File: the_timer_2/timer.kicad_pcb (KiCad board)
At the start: 4 copper layers, 24 x 75 mm, 117 parts, among them J1 Screw_Terminal_01x06, J3 BMI-S-209-F, J4 Screw_Terminal_01x06, J5 R41-B583A, J6 BMI-S-209-F, J7 Screw_Terminal_01x02, Q1 AS2312, Q2 AS2312, Q3 AS2312, Q4 AS2312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

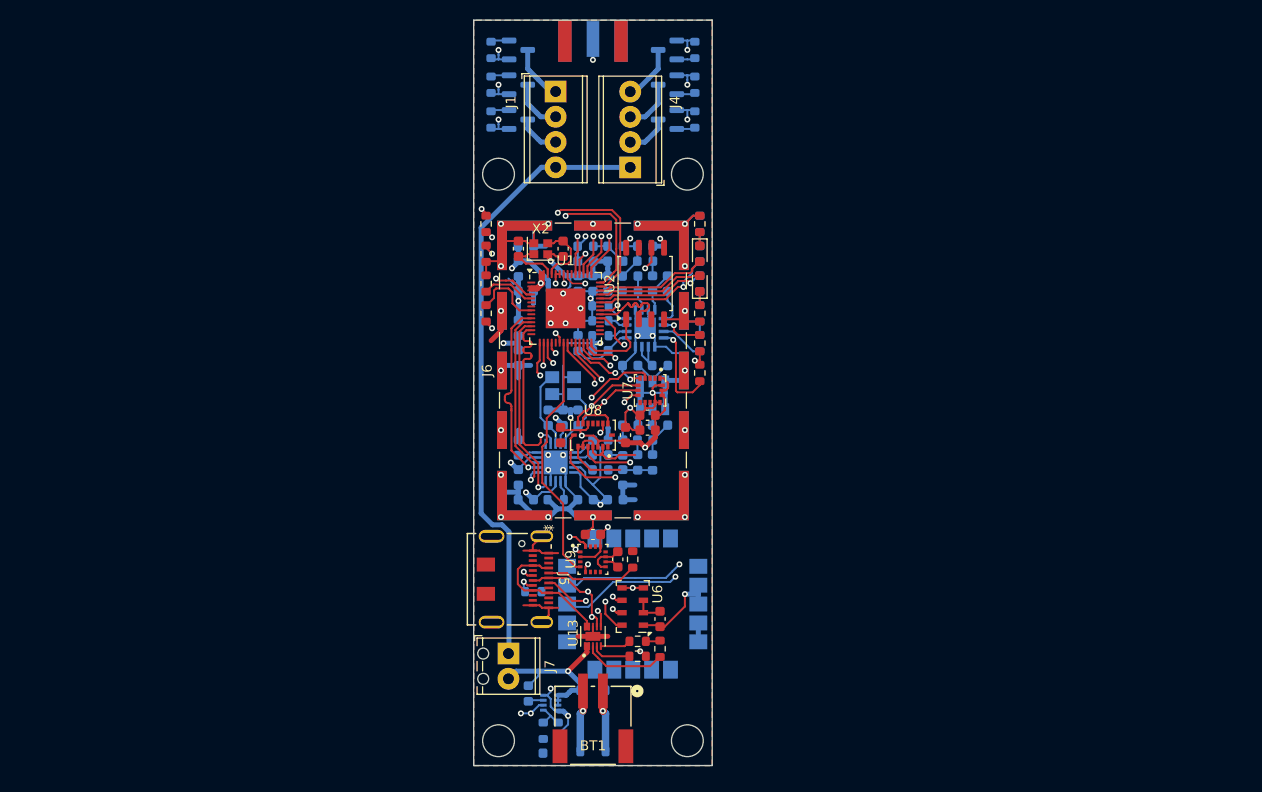
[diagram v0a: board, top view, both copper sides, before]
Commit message: Mostly de-exploded the schematic
Also like sorta fixed the PCB design but not really but sorta
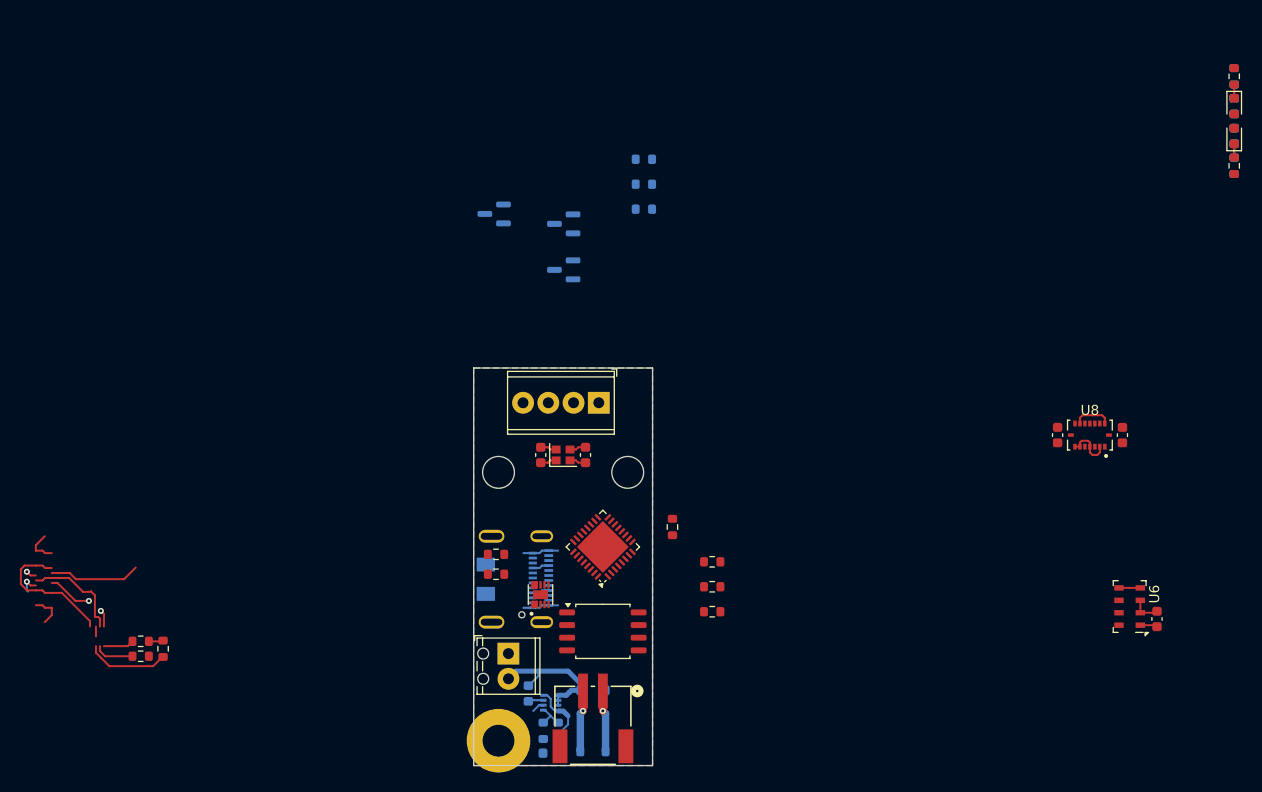
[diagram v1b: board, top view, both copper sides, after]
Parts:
- removed AE1: Conn_Coaxial, Connector_Coaxial:SMA_Samtec_SMA-J-P-X-ST-EM1_EdgeMount
- removed C1, C30, C9: 1u, Capacitor_SMD:C_0603_1608Metric
- removed C10, C2, C8: 10u, Capacitor_SMD:C_0603_1608Metric
- removed C101, C132: 15p, Capacitor_SMD:C_0603_1608Metric
- removed C111, C141, C151, C181, C41, C51, C91: 100n, Capacitor_SMD:C_0603_1608Metric
- removed C121: 1p, Capacitor_SMD:C_0603_1608Metric
- removed C122, C131: 1.5p, Capacitor_SMD:C_0603_1608Metric
- removed C123, C21, C26: 47p, Capacitor_SMD:C_0603_1608Metric
- removed C124: 100p, Capacitor_SMD:C_0603_1608Metric
- removed C125: 0.8p, Capacitor_SMD:C_0603_1608Metric
- removed C161: 27p, Capacitor_SMD:C_0603_1608Metric
- removed C22, C52, C81: 12p, Capacitor_SMD:C_0603_1608Metric
- removed C24: 3.3p, Capacitor_SMD:C_0603_1608Metric
- removed C25: 7.5p, Capacitor_SMD:C_0603_1608Metric
- removed C27: 1n, Capacitor_SMD:C_0603_1608Metric
- removed C28: ???, Capacitor_SMD:C_0603_1608Metric
- removed C3: 220p, Capacitor_SMD:C_0603_1608Metric
- removed C7: 0.1u, Capacitor_SMD:C_0603_1608Metric
- removed H2: MountingHole, MountingHole:MountingHole_3.2mm_M3
- removed J3, J6: BMI-S-209-F, RF_Shielding:Laird_Technologies_BMI-S-209-F_29.36x18.50mm
- removed J4: Screw_Terminal_01x06, TerminalBlock_Phoenix:TerminalBlock_Phoenix_MPT-0,5-4-2.54_1x04_P2.54mm_Horizontal
- removed L1: 1k, Inductor_SMD:L_0603_1608Metric
- removed L121, L131: 12n, Inductor_SMD:L_0603_1608Metric
- removed L122, L132: 18n, Inductor_SMD:L_0603_1608Metric
- removed L130: 1.5n, Inductor_SMD:L_0603_1608Metric
- removed L2: 11n, Inductor_SMD:L_0603_1608Metric
- removed L21: 22n, Inductor_SMD:L_0603_1608Metric
- removed L22: 7.5n, Inductor_SMD:L_0603_1608Metric
- removed L23: 2.9n, Inductor_SMD:L_0603_1608Metric
- removed L24: 9.1n, Inductor_SMD:L_0603_1608Metric
- removed L25: 10n, Inductor_SMD:L_0603_1608Metric
- removed Q4, Q5, Q6: AS2312, Package_TO_SOT_SMD:SOT-23
- removed R10, R11, R12, R13, R20, R21: 10k, Resistor_SMD:R_0603_1608Metric
- removed R141: 3.3k, Resistor_SMD:R_0603_1608Metric
- removed R151: 47, Resistor_SMD:R_0603_1608Metric
- removed R161: 10, Resistor_SMD:R_0603_1608Metric
- removed R171: 56k, Resistor_SMD:R_0603_1608Metric
- removed U11: SAM-M8Q, RF_GPS:ublox_SAM-M8Q
- removed U3: CC1101RGPR, locals_but_working_PLEASE:CC1101RGPR
- removed U4: CC1190RGVR, locals_but_working_PLEASE:CC1190RGVR
- removed U5: B39921B3728U410, Filter:Filter_SAW-6_3.8x3.8mm
- removed U7: H3LIS200DLTR, locals_but_working_PLEASE:H3LIS200DLTR
- removed U9: MMC5883MA, locals_but_working_PLEASE:MMC5983MA
- removed the X1 at (209.0, 61.8)
- H1: value MountingHole -> MountingHole_Pad; footprint MountingHole:MountingHole_3.2mm_M3 -> MountingHole:MountingHole_3.2mm_M3_Pad
- J5: moved to B.Cu
- R25, R5, R7, R9: moved to F.Cu
- U1: value ESP32-S3FN8 -> ESP32-C3FH4; footprint Package_DFN_QFN:QFN-56-1EP_7x7mm_P0.4mm_EP4x4mm -> Package_DFN_QFN:QFN-32-1EP_5x5mm_P0.5mm_EP3.7x3.7mm
- moved R9 56.5 mm to (224.0, 84.5), turned to 0 degrees
- moved D2 55.8 mm to (276.5, 33.7)
- moved D3 55.8 mm to (276.5, 36.7)
- moved D4 55.8 mm to (276.5, 33.7)
- moved D5 55.8 mm to (276.5, 36.7)
- moved R14 55.8 mm to (276.5, 30.7)
- moved R15 55.8 mm to (276.5, 39.7)
- moved R16 55.8 mm to (276.5, 30.7)
- moved R17 55.8 mm to (276.5, 39.7)
- moved R5 52.9 mm to (224.0, 79.5), turned to 0 degrees
- moved C12 50.0 mm to (258.8, 66.8)
- moved C6 50.0 mm to (268.8, 85.2)
- moved R22 50.0 mm to (166.5, 89.0)
- moved R23 50.0 mm to (168.8, 88.2)
- moved R28 50.0 mm to (166.5, 87.5)
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- renumbered X2 to X1
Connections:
- R1 pad 1: PA_EN -> Net-(U1-CHIP_EN)
- R5 pad 1: T_{2} -> Net-(U1-GPIO2)
- R5 pad 2: GND -> VCC
- R6 pad 1: T_{3} -> T_{2}
- R7 pad 1: T_{4} -> Net-(U1-GPIO8)
- R7 pad 2: GND -> VCC
- R8 pad 1: T_{5} -> T_{3}
- R9 pad 1: T_{6} -> Net-(U1-GPIO9)
- U1 pad 1: unconnected-(U1-LNA_IN-Pad1) -> ~{CS}_{GYRO}
- U1 pad 10: SDO3 -> SCL1
- U1 pad 11: SCLK3 -> VCC
- U1 pad 12: SDI3 -> SCLK2
- U1 pad 13: ~{CS}_{RF} -> SDI2
- U1 pad 14: unconnected-(U1-GPIO9-Pad14) -> Net-(U1-GPIO8)
- U1 pad 15: ~{CS}_{MAIN_ACC} -> Net-(U1-GPIO9)
- U1 pad 16: SDI2 -> ~{CS}_{MAIN_ACC}
- U1 pad 17: SCLK2 -> VCC
- U1 pad 18: SDO2 -> VCC
- U1 pad 20: VCC -> unconnected-(U1-SPIWP-Pad20)
- U1 pad 21: ~{CS}_{MAG} -> unconnected-(U1-SPICS0-Pad21)
- U1 pad 22: ~{CS}_{GYRO} -> SCLK1
- U1 pad 23: unconnected-(U1-GPIO17-Pad23) -> SDI1
- U1 pad 24: ~{CS}_{BARO} -> SDO1
- U1 pad 27: ~{CS}_{HI_ACC} -> ~{CS}_{FLASH}
- U1 pad 28: ~{CS}_{FLASH} -> ~{CS}_{BARO}
- U1 pad 29: unconnected-(U1-VDD_SPI-Pad29) -> XTAL_N
- U1 pad 30: unconnected-(U1-SPIHD-Pad30) -> XTAL_P
- U1 pad 31: unconnected-(U1-SPIWP-Pad31) -> VCC
- U1 pad 32: unconnected-(U1-SPICS0-Pad32) -> VCC
- U1 pad 33: SCLK1 -> GND
- U1 pad 4: Net-(U1-CHIP_PU) -> T_{1}
- U1 pad 5: Net-(U1-GPIO0) -> T_{2}
- U1 pad 6: unconnected-(U1-GPIO1-Pad6) -> Net-(U1-GPIO2)
- U1 pad 7: unconnected-(U1-GPIO2-Pad7) -> Net-(U1-CHIP_EN)
- U1 pad 8: Net-(U1-GPIO3) -> SDO2
- U1 pad 9: unconnected-(U1-GPIO4-Pad9) -> SDA1
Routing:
- net GND: track 216.9 -> 28.7 mm, vias 40 -> 0
- net /Inputs Outputs/PYRO: track 62.1 -> 0.00 mm
- net VCC_{CC1101}: track 59.5 -> 0.00 mm, vias 5 -> 0
- net USB_D-: track 62.7 -> 7.26 mm, vias 4 -> 3
- net VCC: track 62.8 -> 9.47 mm, vias 15 -> 0
- net SCLK2: track 50.8 -> 0.00 mm, vias 5 -> 0
- net RXD: track 50.5 -> 0.00 mm, vias 2 -> 0
- net TXD: track 50.0 -> 0.00 mm, vias 2 -> 0
- net USB_D+: track 57.3 -> 10.3 mm, vias 3 -> 0
- net SDI2: track 45.9 -> 0.00 mm, vias 4 -> 0
- net SDO2: track 42.3 -> 3.86 mm, vias 4 -> 0
- net VCC_{CC1190}: track 33.7 -> 0.00 mm, vias 2 -> 0
- net T_{2}: track 31.6 -> 0.00 mm, vias 2 -> 0
- net T_{6}: track 29.7 -> 0.00 mm, vias 2 -> 0
- net T_{3}: track 29.4 -> 0.00 mm, vias 2 -> 0
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- removed copper zone on In1.Cu, net VCC
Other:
- board size 24 x 75 mm -> 18 x 40 mm
- copper layers 4 -> 2
